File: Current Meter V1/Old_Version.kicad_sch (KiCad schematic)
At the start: 18 parts, among them U102 STM32F411RETx, U103 A1308xLHxx-2

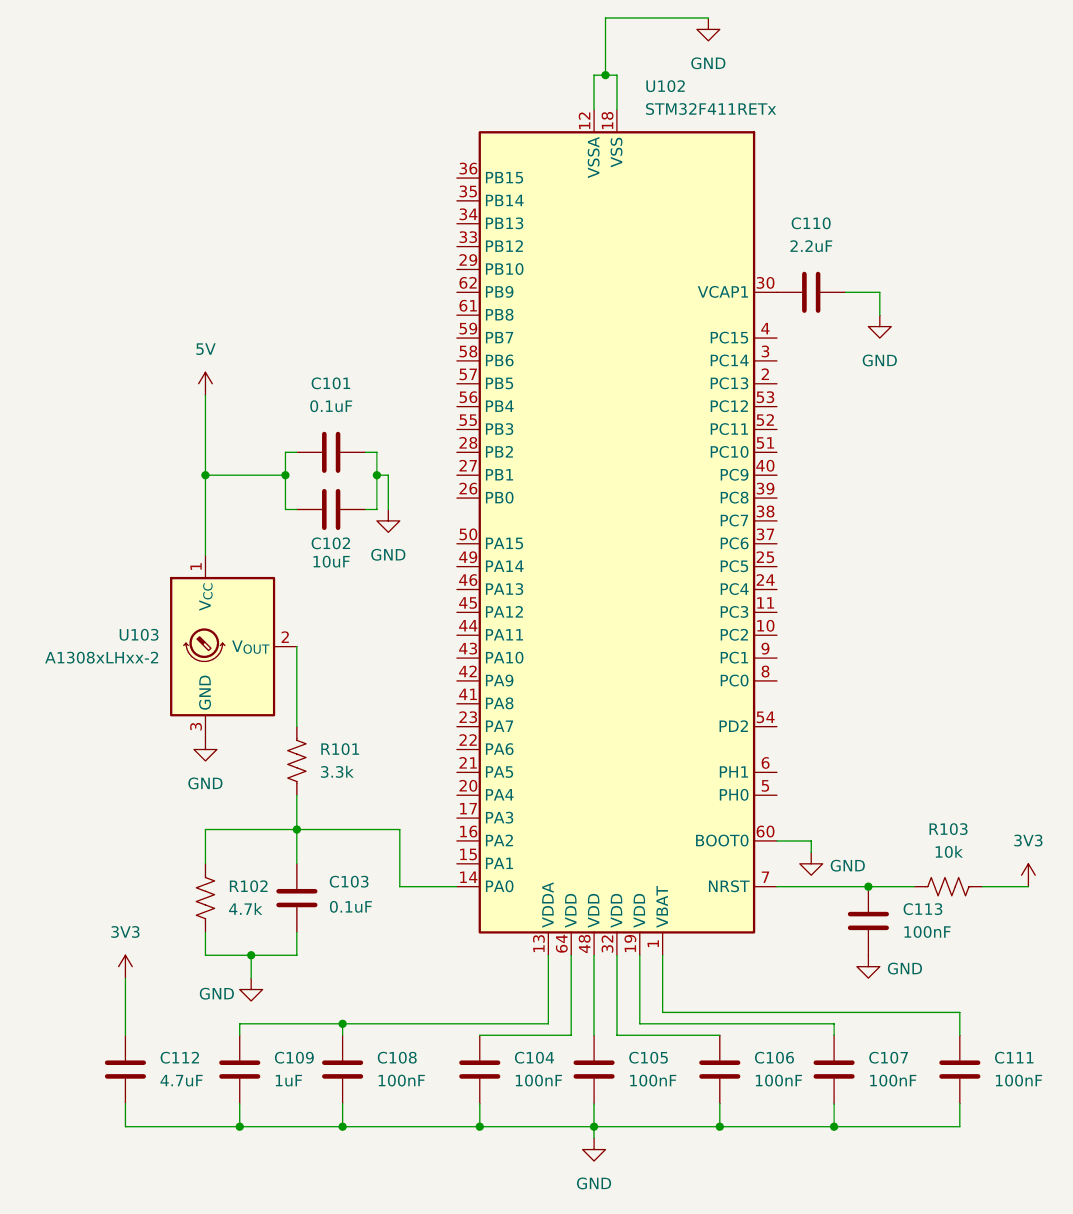
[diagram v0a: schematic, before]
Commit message: Changes Added usb c power, 3v3 ldo, protection diode for hall output, capacitors and power rail on stm
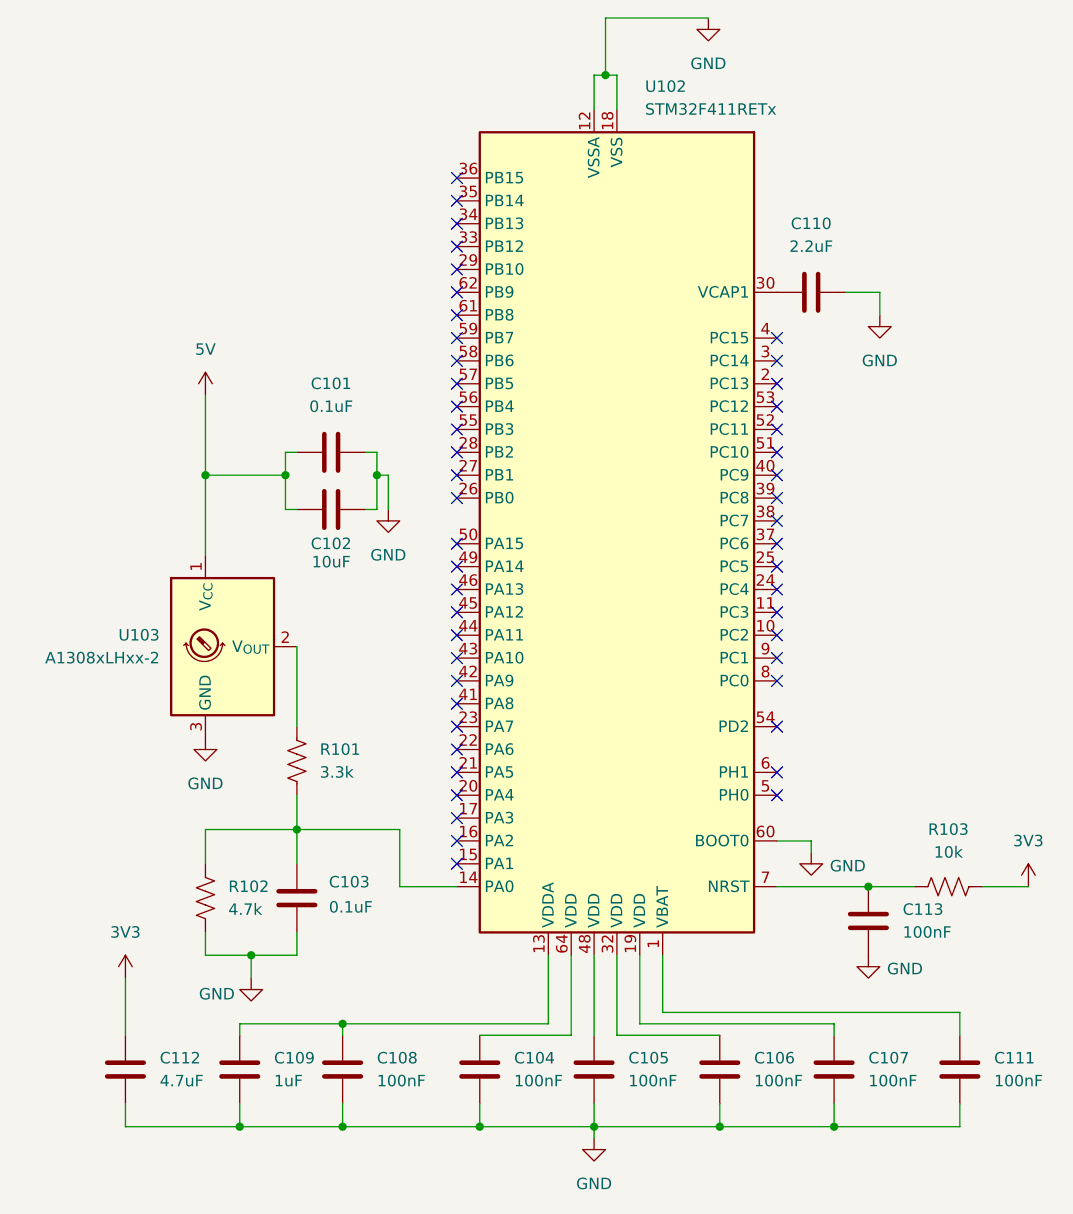
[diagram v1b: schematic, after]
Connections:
- no-connect marks 0 -> 49
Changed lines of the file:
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@@
 		(color 0 0 0 0)
+	)
+	(no_connect
+		(at 179.07 76.2)
+	)
+	(no_connect
+		(at 179.07 111.76)
+	)
+	(no_connect
+		(at 179.07 106.68)
+	)
+	(no_connect
+		(at 143.51 116.84)
+	)
+	(no_connect
+		(at 143.51 81.28)
+	)
+	(no_connect
+		(at 143.51 63.5)
+	)
+	(no_connect
+		(at 143.51 91.44)
+	)
+	(no_connect
+		(at 179.07 116.84)
+	)
+	(no_connect
+		(at 179.07 99.06)
+	)
+	(no_connect
+		(at 143.51 71.12)
+	)
+	(no_connect
+		(at 143.51 83.82)
+	)
+	(no_connect
+		(at 179.07 104.14)
+	)
+	(no_connect
+		(at 179.07 86.36)
+	)
+	(no_connect
+		(at 179.07 119.38)
+	)
+	(no_connect
+		(at 143.51 55.88)
+	)
+	(no_connect
+		(at 143.51 114.3)
+	)
+	(no_connect
+		(at 179.07 88.9)
+	)
+	(no_connect
+		(at 179.07 101.6)
+	)
+	(no_connect
+		(at 143.51 124.46)
+	)
+	(no_connect
+		(at 143.51 53.34)
+	)
+	(no_connect
+		(at 179.07 91.44)
+	)
+	(no_connect
+		(at 179.07 68.58)
+	)
+	(no_connect
+		(at 143.51 101.6)
+	)
+	(no_connect
+		(at 143.51 73.66)
+	)
+	(no_connect
+		(at 179.07 78.74)
+	)
+	(no_connect
+		(at 143.51 86.36)
+	)
+	(no_connect
+		(at 179.07 71.12)
+	)
+	(no_connect
+		(at 143.51 66.04)
+	)
+	(no_connect
+		(at 179.07 73.66)
+	)
+	(no_connect
+		(at 143.51 50.8)
+	)
+	(no_connect
+		(at 143.51 58.42)
+	)
+	(no_connect
+		(at 143.51 96.52)
+	)
+	(no_connect
+		(at 179.07 93.98)
+	)
+	(no_connect
+		(at 143.51 104.14)
+	)
+	(no_connect
+		(at 179.07 81.28)
+	)
+	(no_connect
+		(at 143.51 68.58)
+	)
+	(no_connect
+		(at 143.51 60.96)
+	)
+	(no_connect
+		(at 143.51 106.68)
+	)
+	(no_connect
+		(at 143.51 109.22)
+	)
+	(no_connect
+		(at 143.51 119.38)
+	)
+	(no_connect
+		(at 179.07 96.52)
+	)
+	(no_connect
+		(at 143.51 99.06)
+	)
+	(no_connect
+		(at 143.51 111.76)
+	)
+	(no_connect
+		(at 143.51 76.2)
+	)
+	(no_connect
+		(at 143.51 127)
+	)
+	(no_connect
+		(at 143.51 78.74)
+	)
+	(no_connect
+		(at 143.51 93.98)
+	)
+	(no_connect
+		(at 179.07 83.82)
+	)
+	(no_connect
+		(at 143.51 121.92)
 	)
 	(wire
